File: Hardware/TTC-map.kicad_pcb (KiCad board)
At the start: 2 copper layers, 110 x 60 mm, 35 parts, among them J1 USB_C_Receptacle_USB2.0_16P, Q1 PMOS, Q2 PMOS, Q3 PMOS, Q4 PMOS, Q5 PMOS, Q7 PMOS, U1 ESP32-DEVKIT-V1, U2 74HC595, U3 74HC595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

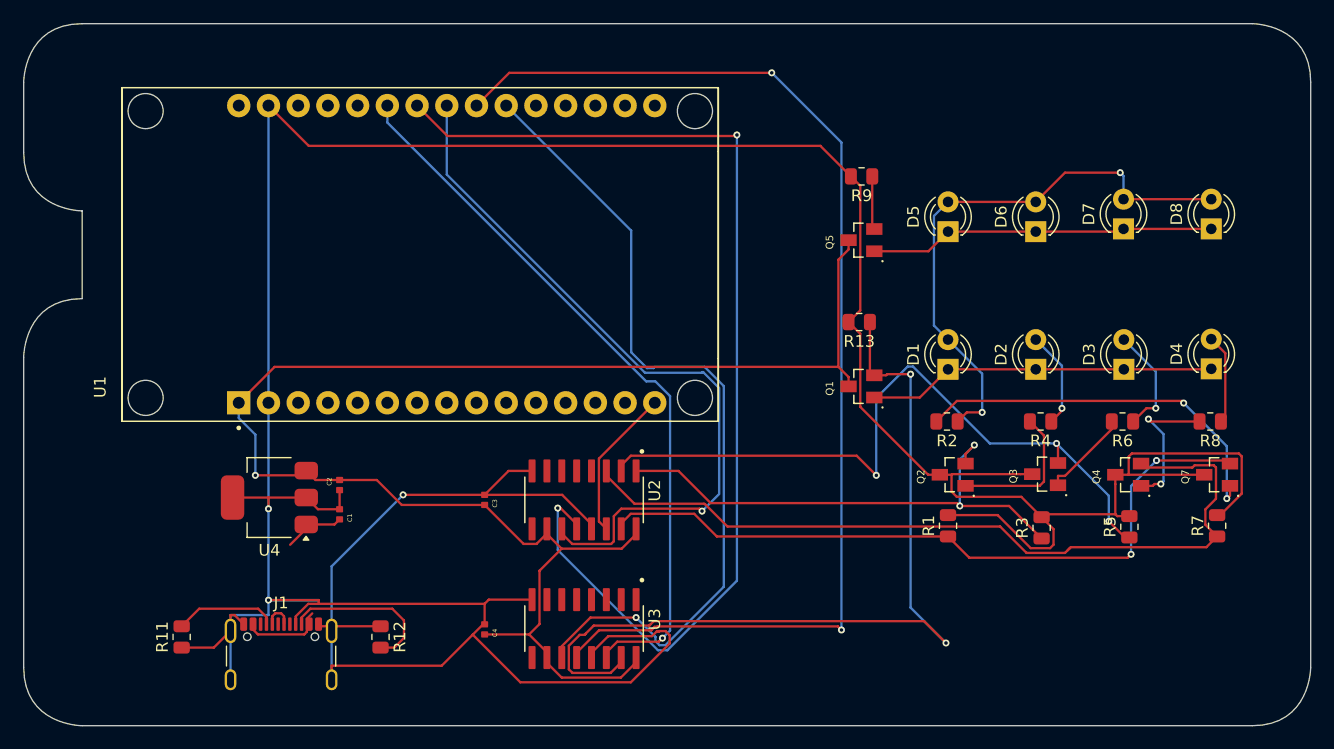
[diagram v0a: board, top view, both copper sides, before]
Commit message: Rerouted the PCB
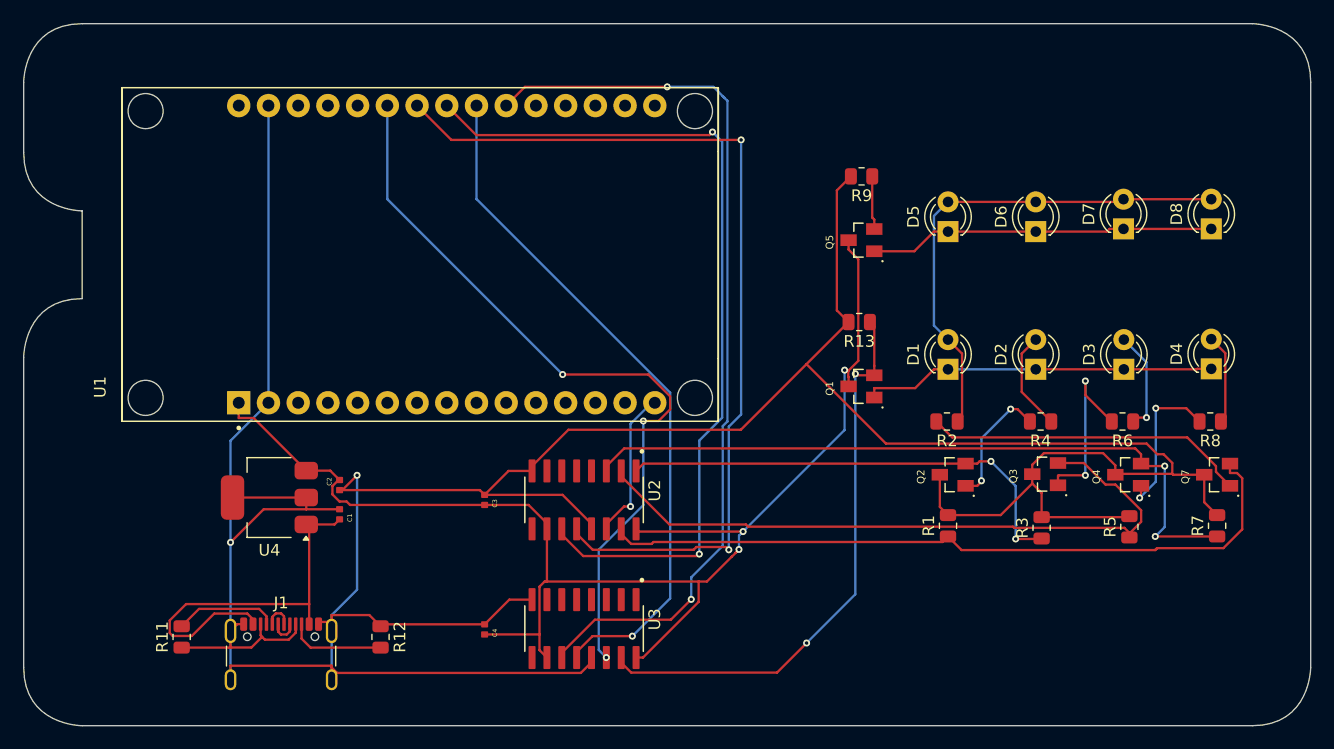
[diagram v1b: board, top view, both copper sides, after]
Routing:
- net /RCLK-2: track 100.7 -> 59.3 mm, vias 2 -> 1
- net GND: track 349.0 -> 313.2 mm, vias 3 -> 2
- net /QA-2: track 73.6 -> 48.8 mm
- net +5V: track 12.4 -> 33.8 mm
- net +3.3V: track 135.2 -> 119.0 mm, vias 1 -> 3
- net /RCLK-1: track 94.0 -> 78.6 mm
- net /SRCLK-1: track 63.3 -> 74.2 mm, vias 1 -> 2
- net Net-(Q3-D): track 7.71 -> 15.6 mm, vias 0 -> 2
- net /QD-1: track 69.5 -> 61.7 mm, vias 0 -> 2
- net /SRCLK-2: track 70.9 -> 77.5 mm, vias 1 -> 2
- net Net-(J1-CC2): track 13.9 -> 8.31 mm
- net /N2: track 48.2 -> 43.0 mm, vias 2 -> 0
- net Net-(Q7-D): track 32.8 -> 27.7 mm, vias 2 -> 0
- net /QC-1: track 61.7 -> 57.4 mm, vias 3 -> 0
- net /QB-1: track 44.7 -> 40.4 mm
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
